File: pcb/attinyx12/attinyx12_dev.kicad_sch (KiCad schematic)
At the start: 26 parts, among them J1 USB_C_Receptacle_USB2.0_16P, J2 Conn_01x06, J3 Conn_01x06, J4 Conn_02x05_Odd_Even, U1 DT1042-04SO, U2 ATtiny212-SS, U3 CH342K

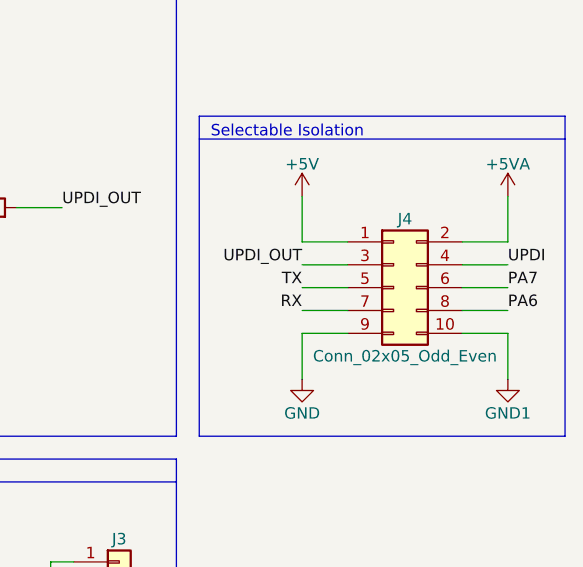
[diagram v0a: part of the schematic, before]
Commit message: flip isolation connector
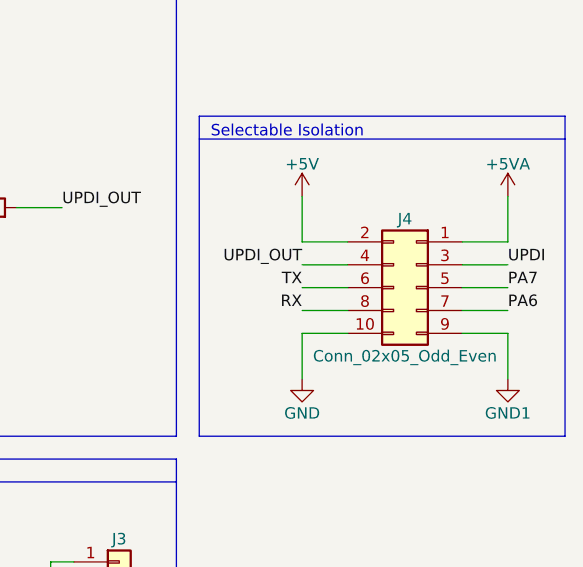
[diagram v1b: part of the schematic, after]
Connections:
- net +5V: now also J4.2 (Pin_2); no longer J4.1 (Pin_1)
- net +5VA: now also J4.1 (Pin_1); no longer J4.2 (Pin_2)
- net GND: now also J4.10 (Pin_10); no longer J4.9 (Pin_9)
- net GND1: now also J4.9 (Pin_9); no longer J4.10 (Pin_10)
- net PA6: now also J4.7 (Pin_7); no longer J4.8 (Pin_8)
- net PA7: now also J4.5 (Pin_5); no longer J4.6 (Pin_6)
- net RX: now also J4.8 (Pin_8); no longer J4.7 (Pin_7)
- net TX: now also J4.6 (Pin_6); no longer J4.5 (Pin_5)
- net UPDI: now also J4.3 (Pin_3); no longer J4.4 (Pin_4)
- net UPDI_OUT: now also J4.4 (Pin_4); no longer J4.3 (Pin_3)
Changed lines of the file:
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@@
 	(symbol
 		(lib_id "Connector_Generic:Conn_02x05_Odd_Even")
-		(at 232.41 57.15 0)
+		(at 234.95 57.15 0)
+		(mirror y)
 		(unit 1)
 		(exclude_from_sim no)
@@
 		)
 		(property "Footprint" "Connector_PinHeader_2.54mm:PinHeader_2x05_P2.54mm_Vertical"
-			(at 232.41 57.15 0)
+			(at 234.95 57.15 0)
 			(effects
 				(font
@@
 		)
 		(property "Datasheet" "~"
-			(at 232.41 57.15 0)
+			(at 234.95 57.15 0)
 			(effects
 				(font
@@
 		)
 		(property "Description" "Generic connector, double row, 02x05, odd/even pin numbering scheme (row 1 odd numbers, row 2 even numbers), script generated (kicad-library-utils/schlib/autogen/connector/)"
-			(at 232.41 57.15 0)
+			(at 234.95 57.15 0)
 			(effects
 				(font

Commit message: update
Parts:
- removed U1: DT1042-04SO, Package_TO_SOT_SMD:SOT-23-6, symbol pl_TVS:DT1042-04SO
- added U1: USBLC6-2SC6, Package_TO_SOT_SMD:SOT-23-6, symbol Power_Protection:USBLC6-2SC6
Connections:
- net D+: now also U1.3 (I/O2); no longer U3.1 (UD+)
- net D-: now also U1.1 (I/O1); no longer U3.2 (UD-)
- net GND: now also U1.2 (GND)
- net PA6: now also J4.5 (Pin_5); no longer J4.7 (Pin_7)
- net PA7: now also J4.3 (Pin_3); no longer J4.5 (Pin_5)
- net RX: now also J4.6 (Pin_6); no longer J4.8 (Pin_8)
- net TX: now also J4.4 (Pin_4); no longer J4.6 (Pin_6)
- net UPDI: now also J4.7 (Pin_7); no longer J4.3 (Pin_3)
- net UPDI_OUT: now also J4.8 (Pin_8); no longer J4.4 (Pin_4)
- net VBUS: now also U1.5 (VBUS)
- new net UD+: U1.4 (I/O2), U3.1 (UD+)
- new net UD-: U1.6 (I/O1), U3.2 (UD-)
- no-connect marks 4 -> 2
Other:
- moved on the sheet: D2, F1

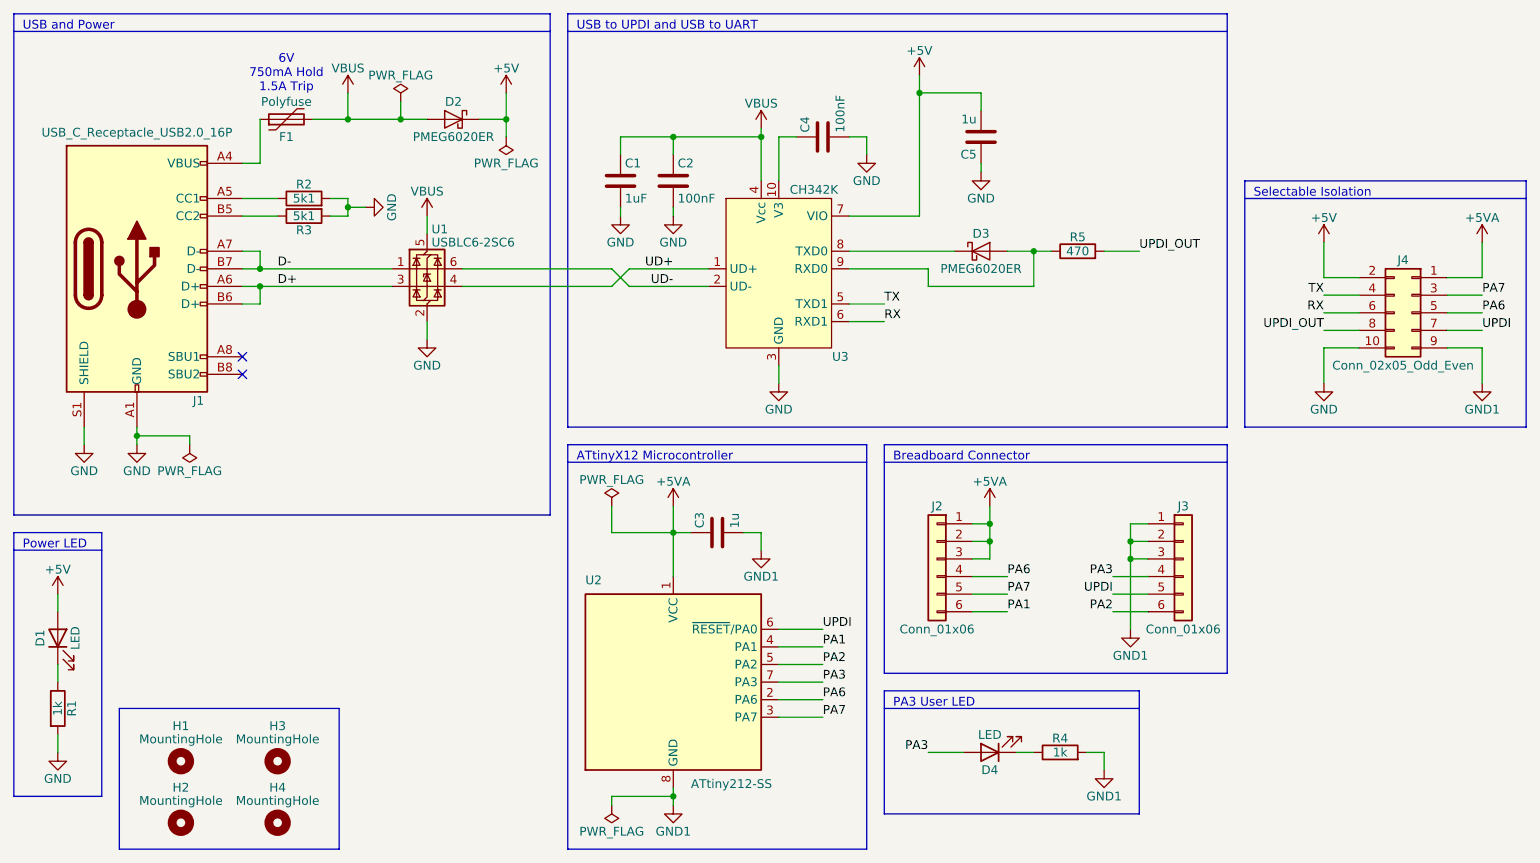
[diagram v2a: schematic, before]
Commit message: remove 2 mounting holes
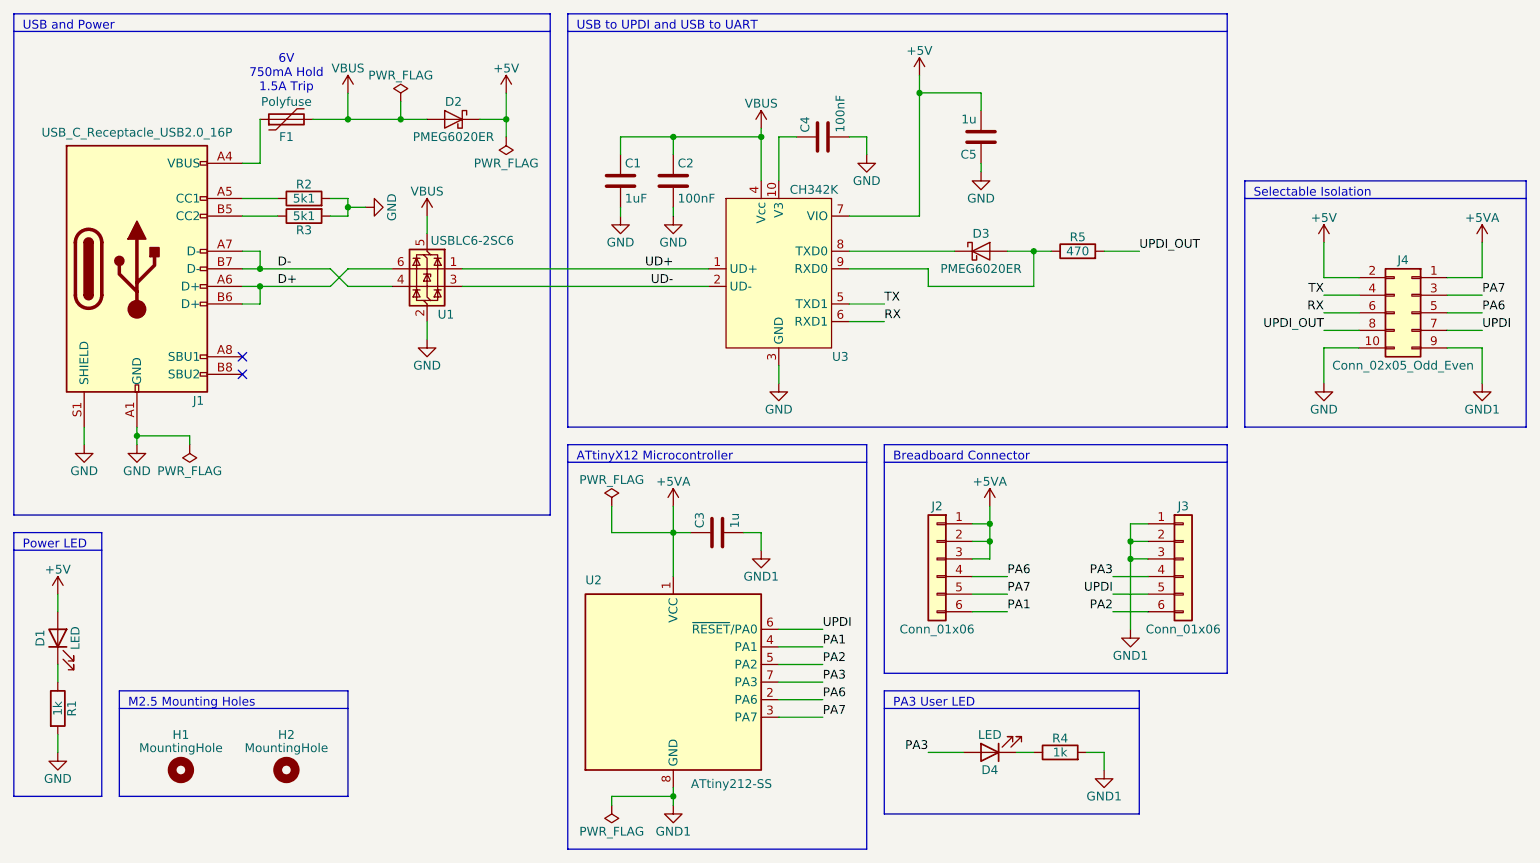
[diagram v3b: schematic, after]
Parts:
- removed H3, H4: MountingHole, MountingHole:MountingHole_2.7mm_M2.5, symbol Mechanical:MountingHole
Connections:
- net D+: now also U1.6 (I/O1); no longer U1.3 (I/O2)
- net D-: now also U1.4 (I/O2); no longer U1.1 (I/O1)
- net UD+: now also U1.1 (I/O1); no longer U1.4 (I/O2)
- net UD-: now also U1.3 (I/O2); no longer U1.6 (I/O1)
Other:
- note added: "M2.5 Mounting Holes"
- moved on the sheet: H1, H2
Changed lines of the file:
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@@
 	(wire
 		(pts
+			(xy 81.28 53.34) (xy 87.63 53.34)
+		)
+		(stroke
+			(width 0)
+			(type default)
+		)
+	)
+	(wire
+		(pts
 			(xy 143.51 105.41) (xy 149.86 105.41)
 		)
@@
 	(wire
 		(pts
-			(xy 119.38 53.34) (xy 121.92 50.8)
+			(xy 78.74 53.34) (xy 81.28 50.8)
 		)
 		(stroke
@@
 	(wire
 		(pts
+			(xy 81.28 50.8) (xy 87.63 50.8)
+		)
+		(stroke
+			(width 0)
+			(type default)
+		)
+	)
+	(wire
+		(pts
 			(xy 66.04 35.56) (xy 68.58 35.56)
 		)
@@
 	(wire
 		(pts
-			(xy 68.58 53.34) (xy 87.63 53.34)
+			(xy 68.58 53.34) (xy 78.74 53.34)
 		)
 		(stroke
@@
 	(wire
 		(pts
-			(xy 119.38 50.8) (xy 121.92 53.34)
+			(xy 78.74 50.8) (xy 81.28 53.34)
 		)
 		(stroke
@@
 	(wire
 		(pts
-			(xy 97.79 53.34) (xy 119.38 53.34)
+			(xy 97.79 53.34) (xy 133.35 53.34)
 		)
 		(stroke
@@
 		)
 	)
-	(wire
-		(pts
-			(xy 121.92 50.8) (xy 133.35 50.8)
-		)
-		(stroke
-			(width 0)
-			(type default)
-		)
-	)
-	(wire
+	(polyline
 		(pts
-			(xy 121.92 53.34) (xy 133.35 53.34)
+			(xy 48.26 114.3) (xy 81.28 114.3)
 		)
 		(stroke
@@
 	(wire
 		(pts
-			(xy 68.58 50.8) (xy 87.63 50.8)
+			(xy 68.58 50.8) (xy 78.74 50.8)
 		)
 		(stroke
@@
 	(wire
 		(pts
-			(xy 97.79 50.8) (xy 119.38 50.8)
+			(xy 97.79 50.8) (xy 133.35 50.8)
 		)
 		(stroke
@@
 	)
 	(rectangle
-		(start 48.26 114.3)
-		(end 80.01 134.62)
+		(start 48.26 111.76)
+		(end 81.28 127)
 		(stroke
 			(width 0)
@@
 		)
 	)
+	(text "M2.5 Mounting Holes"
+		(exclude_from_sim no)
+		(at 49.53 114.3 0)
+		(effects
+			(font
+				(size 1.27 1.27)
+			)
+			(justify left bottom)
+		)
+	)
 	(text "USB to UPDI and USB to UART"
 		(exclude_from_sim no)
@@
 		(lib_id "Power_Protection:USBLC6-2SC6")
 		(at 92.71 50.8 0)
+		(mirror y)
 		(unit 1)
 		(exclude_from_sim no)
@@
 		(dnp no)
 		(property "Reference" "U1"
-			(at 93.345 45.085 0)
+			(at 94.234 57.404 0)
 			(effects
 				(font
 					(size 1.27 1.27)
 				)
-				(justify left)
+				(justify right)
 			)
 		)
 		(property "Value" "USBLC6-2SC6"
-			(at 93.345 46.99 0)
+			(at 93.218 46.736 0)
 			(effects
 				(font
 					(size 1.27 1.27)
 				)
-				(justify left)
+				(justify right)
 			)
 		)
 		(property "Footprint" "Package_TO_SOT_SMD:SOT-23-6"
-			(at 93.98 57.15 0)
+			(at 91.44 57.15 0)
 			(effects
 				(font
@@
 		)
 		(property "Datasheet" "https://www.st.com/resource/en/datasheet/usblc6-2.pdf"
-			(at 93.98 59.055 0)
+			(at 91.44 59.055 0)
 			(effects
 				(font
@@
 	(symbol
 		(lib_id "Mechanical:MountingHole")
-		(at 57.15 121.92 0)
+		(at 57.15 123.19 0)
 		(unit 1)
 		(exclude_from_sim yes)
@@
 		(dnp no)
 		(property "Reference" "H1"
-			(at 57.15 116.84 0)
+			(at 57.15 118.11 0)
 			(effects
 				(font
@@
 		)
 		(property "Value" "MountingHole"
-			(at 57.15 118.745 0)
+			(at 57.15 120.015 0)
 			(effects
 				(font
@@
 		)
 		(property "Footprint" "MountingHole:MountingHole_2.7mm_M2.5"
-			(at 57.15 121.92 0)
+			(at 57.15 123.19 0)
 			(effects
 				(font
@@
 		)
 		(property "Datasheet" "~"
-			(at 57.15 121.92 0)
+			(at 57.15 123.19 0)
 			(effects
 				(font
@@
 		)
 		(property "Description" "Mounting Hole without connection"
-			(at 57.15 121.92 0)
+			(at 57.15 123.19 0)
 			(effects
 				(font
@@
 	)
 	(symbol
-		(lib_id "Mechanical:MountingHole")
-		(at 71.12 130.81 0)
-		(unit 1)
-		(exclude_from_sim yes)
-		(in_bom no)
-		(on_board yes)
-		(dnp no)
-		(property "Reference" "H4"
-			(at 71.12 125.73 0)
-			(effects
-				(font
-					(size 1.27 1.27)
-				)
-			)
-		)
-		(property "Value" "MountingHole"
-			(at 71.12 127.635 0)
-			(effects
-				(font
-					(size 1.27 1.27)
-				)
-			)
-		)
-		(property "Footprint" "MountingHole:MountingHole_2.7mm_M2.5"
-			(at 71.12 130.81 0)
-			(effects
-				(font
-					(size 1.27 1.27)
-				)
-				(hide yes)
-			)
-		)
-		(property "Datasheet" "~"
-			(at 71.12 130.81 0)
-			(effects
-				(font
-					(size 1.27 1.27)
-				)
-				(hide yes)
-			)
-		)
-		(property "Description" "Mounting Hole without connection"
-			(at 71.12 130.81 0)
-			(effects
-				(font
-					(size 1.27 1.27)
-				)
-				(hide yes)
-			)
-		)
-		(instances
-			(project "attinyx12_dev"
-				(path "/0b8e28b0-653e-4072-b0e8-3e5a3c288af6"
-					(reference "H4")
-					(unit 1)
-				)
-			)
-		)
-	)
-	(symbol
 		(lib_id "power:GND1")
 		(at 140.97 91.44 0)
@@
 	(symbol
 		(lib_id "Mechanical:MountingHole")
-		(at 57.15 130.81 0)
+		(at 72.39 123.19 0)
 		(unit 1)
 		(exclude_from_sim yes)
@@
 		(dnp no)
 		(property "Reference" "H2"
-			(at 57.15 125.73 0)
+			(at 72.39 118.11 0)
 			(effects
 				(font
@@
 		)
 		(property "Value" "MountingHole"
-			(at 57.15 127.635 0)
+			(at 72.39 120.015 0)
 			(effects
 				(font
@@
 		)
 		(property "Footprint" "MountingHole:MountingHole_2.7mm_M2.5"
-			(at 57.15 130.81 0)
+			(at 72.39 123.19 0)
 			(effects
 				(font
@@
 		)
 		(property "Datasheet" "~"
-			(at 57.15 130.81 0)
+			(at 72.39 123.19 0)
 			(effects
 				(font
@@
 		)
 		(property "Description" "Mounting Hole without connection"
-			(at 57.15 130.81 0)
+			(at 72.39 123.19 0)
 			(effects
 				(font
@@
 					(unit 1)
 				)
-			)
-		)
-	)
-	(symbol
-		(lib_id "Mechanical:MountingHole")
-		(at 71.12 121.92 0)
-		(unit 1)
-		(exclude_from_sim yes)
-		(in_bom no)
-		(on_board yes)
-		(dnp no)
-		(property "Reference" "H3"
-			(at 71.12 116.84 0)
-			(effects
-				(font
-					(size 1.27 1.27)
-				)
-			)
-		)
-		(property "Value" "MountingHole"
-			(at 71.12 118.745 0)
-			(effects
-				(font
-					(size 1.27 1.27)
-				)
-			)
-		)
-		(property "Footprint" "MountingHole:MountingHole_2.7mm_M2.5"
-			(at 71.12 121.92 0)
-			(effects
-				(font
-					(size 1.27 1.27)
-				)
-				(hide yes)
-			)
-		)
-		(property "Datasheet" "~"
-			(at 71.12 121.92 0)
-			(effects
-				(font
-					(size 1.27 1.27)
-				)
-				(hide yes)
-			)
-		)
-		(property "Description" "Mounting Hole without connection"
-			(at 71.12 121.92 0)
-			(effects
-				(font
-					(size 1.27 1.27)
-				)
-				(hide yes)
-			)
-		)
-		(instances
-			(project "attinyx12_dev"
-				(path "/0b8e28b0-653e-4072-b0e8-3e5a3c288af6"
-					(reference "H3")
-					(unit 1)
-				)

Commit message: user LED on programmer side
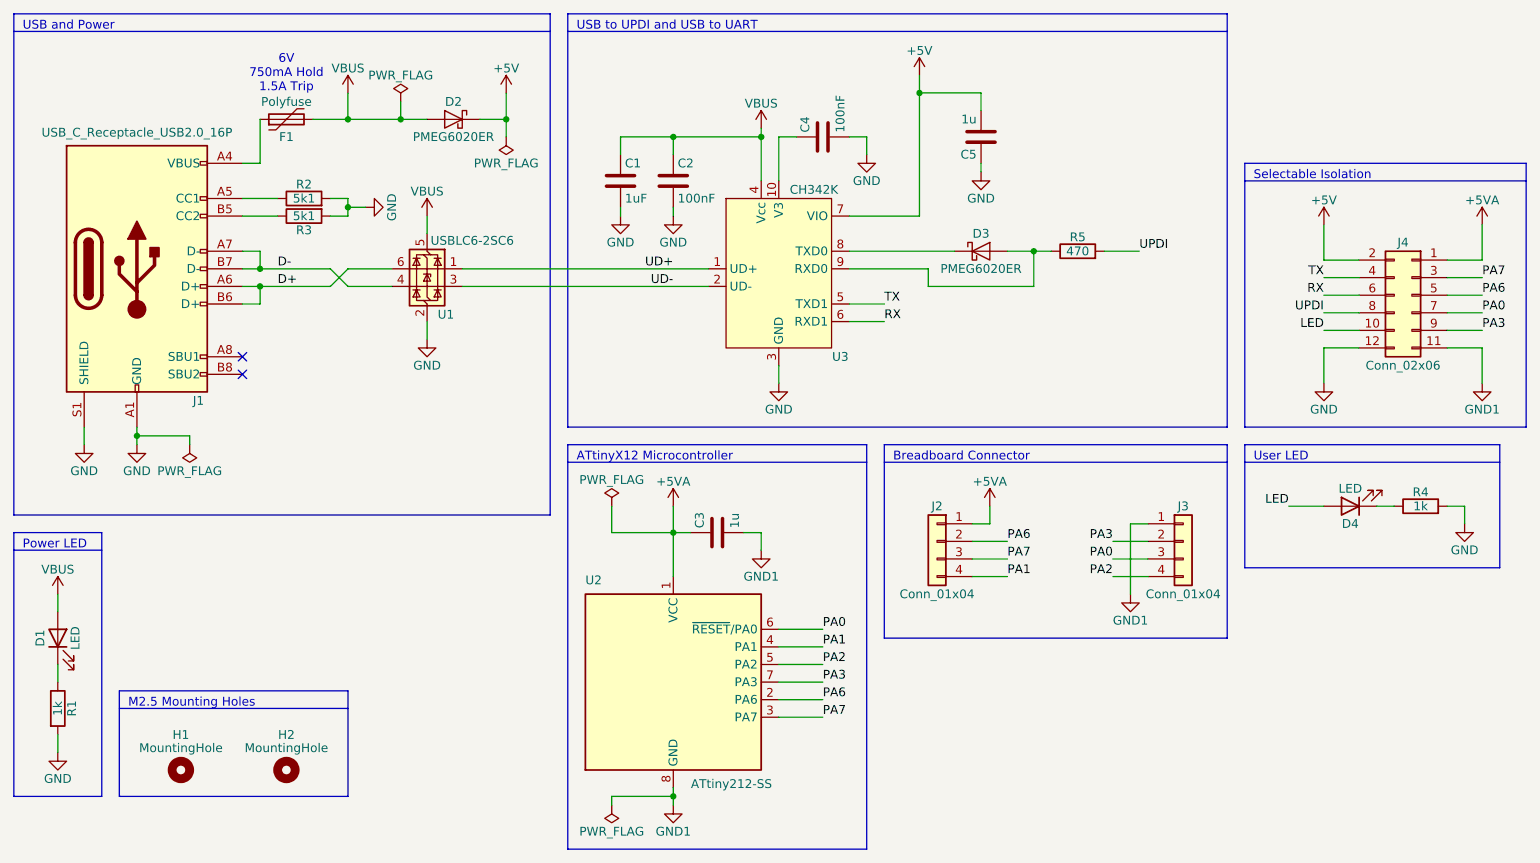
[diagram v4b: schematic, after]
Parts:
- removed J2, J3: Conn_01x06, Connector_PinHeader_2.54mm:PinHeader_1x06_P2.54mm_Vertical, symbol Connector_Generic:Conn_01x06
- added J2, J3: Conn_01x04, Connector_PinHeader_2.54mm:PinHeader_1x04_P2.54mm_Vertical, symbol Connector_Generic:Conn_01x04
- J4: value Conn_02x05_Odd_Even -> Conn_02x06; footprint Connector_PinHeader_2.54mm:PinHeader_2x05_P2.54mm_Vertical -> Connector_PinHeader_2.54mm:PinHeader_2x06_P2.54mm_Vertical; symbol Connector_Generic:Conn_02x05_Odd_Even -> Connector_Generic:Conn_02x06_Odd_Even
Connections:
- net UPDI_OUT is gone; now on net UPDI: J4.8 (Pin_8), R5.2
- net +5V: no longer D1.2 (A)
- net +5VA: now also J2.1 (Pin_1)
- net GND: now also J4.12 (Pin_12), R4.2; no longer J4.10 (Pin_10)
- net GND1: now also J4.11 (Pin_11), J3.1 (Pin_1); no longer J4.9 (Pin_9), R4.2
- net PA1: now also J2.4 (Pin_4)
- net PA2: now also J3.4 (Pin_4)
- net PA3: now also J4.9 (Pin_9), J3.2 (Pin_2); no longer D4.2 (A)
- net PA6: now also J2.2 (Pin_2)
- net PA7: now also J2.3 (Pin_3)
- net UPDI: no longer J4.7 (Pin_7), U2.6 (~{RESET}/PA0)
- net VBUS: now also D1.2 (A)
- new net LED: D4.2 (A), J4.10 (Pin_10)
- new net PA0: J3.3 (Pin_3), J4.7 (Pin_7), U2.6 (~{RESET}/PA0)
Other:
- note added: "User LED"
- note removed: "PA3 User LED"
- moved on the sheet: D4, R4

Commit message: final layout
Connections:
- net GND: now also D1.1 (K); no longer R1.2
- net VBUS: now also R1.1; no longer D1.2 (A)
- new net: D1.2 (A), R1.2
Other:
- moved on the sheet: D1, R1
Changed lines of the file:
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@@
 	(title_block
 		(title "ATtinyX12 Development Board")
-		(date "2025-02-17")
+		(date "2025-02-22")
 		(company "Perry Leumas")
 	)
@@
 	(symbol
 		(lib_id "Device:R")
-		(at 39.37 114.3 0)
+		(at 39.37 104.14 0)
 		(unit 1)
 		(exclude_from_sim no)
@@
 		(dnp no)
 		(property "Reference" "R1"
-			(at 41.402 114.3 90)
+			(at 41.402 104.14 90)
 			(effects
 				(font
@@
 		)
 		(property "Value" "1k"
-			(at 39.37 114.3 90)
+			(at 39.37 104.14 90)
 			(effects
 				(font
@@
 		)
 		(property "Footprint" "Resistor_SMD:R_0603_1608Metric"
-			(at 37.592 114.3 90)
+			(at 37.592 104.14 90)
 			(effects
 				(font
@@
 		)
 		(property "Datasheet" "~"
-			(at 39.37 114.3 0)
+			(at 39.37 104.14 0)
 			(effects
 				(font
@@
 		)
 		(property "Description" ""
-			(at 39.37 114.3 0)
+			(at 39.37 104.14 0)
 			(effects
 				(font
@@
 		)
 		(property "MPN" ""
-			(at 39.37 114.3 0)
+			(at 39.37 104.14 0)
 			(effects
 				(font
@@
 		)
 		(property "Manufacture" ""
-			(at 39.37 114.3 0)
+			(at 39.37 104.14 0)
 			(effects
 				(font
@@
 		)
 		(property "SPN" ""
-			(at 39.37 114.3 0)
+			(at 39.37 104.14 0)
 			(effects
 				(font
@@
 		)
 		(property "Supplier" ""
-			(at 39.37 114.3 0)
+			(at 39.37 104.14 0)
 			(effects
 				(font
@@
 		)
 		(property "Tolerance" ""
-			(at 39.37 114.3 0)
+			(at 39.37 104.14 0)
 			(effects
 				(font
@@
 		)
 		(property "Voltage" ""
-			(at 39.37 114.3 0)
+			(at 39.37 104.14 0)
 			(effects
 				(font
@@
 		)
 		(property "Power" ""
-			(at 39.37 114.3 0)
+			(at 39.37 104.14 0)
 			(effects
 				(font
@@
 	(symbol
 		(lib_id "Device:LED")
-		(at 39.37 104.14 90)
+		(at 39.37 114.3 90)
 		(unit 1)
 		(exclude_from_sim no)
@@
 		(dnp no)
 		(property "Reference" "D1"
-			(at 36.83 104.14 0)
+			(at 36.83 114.3 0)
 			(effects
 				(font
@@
 		)
 		(property "Value" "LED"
-			(at 41.91 104.14 0)
+			(at 41.91 114.3 0)
 			(effects
 				(font
@@
 		)
 		(property "Footprint" "LED_SMD:LED_0603_1608Metric"
-			(at 39.37 104.14 0)
+			(at 39.37 114.3 0)
 			(effects
 				(font
@@
 		)
 		(property "Datasheet" "~"
-			(at 39.37 104.14 0)
+			(at 39.37 114.3 0)
 			(effects
 				(font
@@
 		)
 		(property "Description" ""
-			(at 39.37 104.14 0)
+			(at 39.37 114.3 0)
 			(effects
 				(font
